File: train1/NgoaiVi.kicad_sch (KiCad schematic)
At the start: 21 parts, among them IC1 RTC_DS3231M, J4 USB_A_Stacked, J6 MiSD-PP-9P-V1, Q1 SI2300/SOT23-3

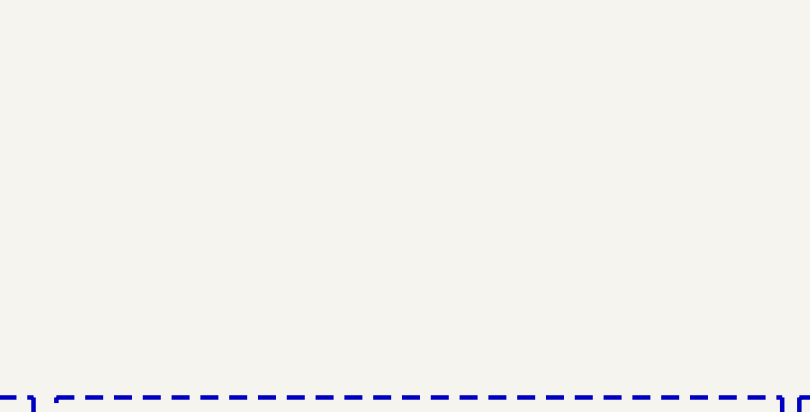
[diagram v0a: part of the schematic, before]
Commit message: fix(repo): delete backup file
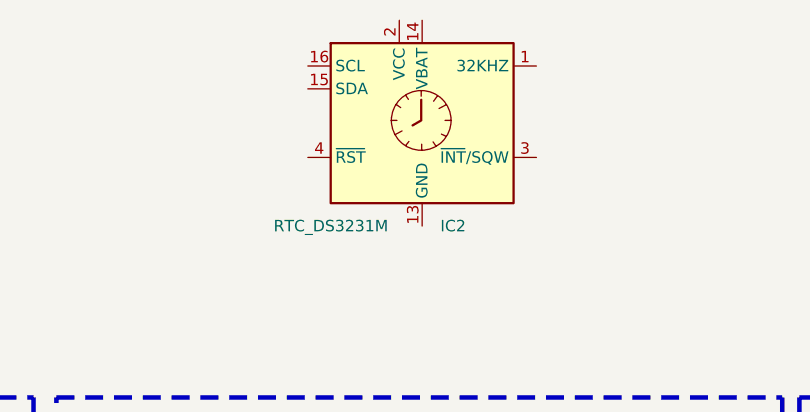
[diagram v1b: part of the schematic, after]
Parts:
- added IC2: RTC_DS3231M, trainFootprint:SOIC-16W_7.5x10.3mm_P1.27mm, symbol TrainSymbol:RTC_DS3231M
- JP2: now left out of the parts list
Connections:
- new net: IC2.10 (GND), IC2.11 (GND), IC2.12 (GND), IC2.13 (GND), IC2.5 (GND), IC2.6 (GND), IC2.7 (GND), IC2.8 (GND), IC2.9 (GND)
